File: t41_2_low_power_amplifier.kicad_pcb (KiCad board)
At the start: 2 copper layers, 100 x 76.2 mm, 61 parts, among them J1 5-1814832-1, J2 5-1814832-1, J3 B2B-XH-A_LF__SN_, J5 Screw_Terminal_01x02, Q1 Q_NPN_BCE, Q4 Q_NPN_BCE, Q5 Q_PMOS_GSD, Q6 Q_NPN_BEC, Q7 Q_NPN_BEC, Q8 Q_NPN_BEC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

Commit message: First version complete and sent to fab.
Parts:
- removed L2: ~, Binocular_Core:BN-43-202_VERTICAL
- added Q2: Q_NPN_BEC, Package_TO_SOT_SMD:SOT-23-3, F.Cu at (154.7, 96.6)
- added Q3: Q_PMOS_GSD, Package_TO_SOT_SMD:SOT-23-3, F.Cu at (160.1, 95.5)
- added R14: 10k, Resistor_SMD:R_1206_3216Metric, F.Cu at (132.5, 93.0)
- added R24: 10k, Resistor_SMD:R_1206_3216Metric, F.Cu at (149.2, 95.6)
- added R27: 10k, Resistor_SMD:R_1206_3216Metric, F.Cu at (159.5, 99.6)
- moved J1 16.0 mm to (187.1, 71.5)
- moved T1 12.3 mm to (172.6, 74.5)
- moved C1 2.61 mm to (168.3, 74.5), turned to 0 degrees
- moved C18 0.72 mm to (143.9, 60.4), turned to 180 degrees
- moved C15 0.25 mm to (125.9, 76.1)
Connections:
- C1 pad 1: /12V_IN_FIL -> /12V_FINAL
- T1 pad 4: /12V_IN_FIL -> /12V_FINAL
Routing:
- net /8V: track 9.43 -> 43.3 mm
- net /12V_FINAL: track 0.00 -> 27.0 mm
- net /12V: track 51.6 -> 75.9 mm
- net Net-(T1-AB): track 0.00 -> 6.57 mm
- net Net-(Q2-C): track 0.00 -> 6.32 mm
- net Net-(Q7-C): track 12.5 -> 18.6 mm
- net Net-(R11-Pad2): track 0.00 -> 4.71 mm
- net /TXRX: track 44.8 -> 48.5 mm
- net Net-(Q4-C): track 4.50 -> 7.95 mm
- net Net-(Q1-C): track 4.55 -> 7.97 mm
- net Net-(T3-AB): track 0.00 -> 3.28 mm
- net Net-(T3-SB): track 0.00 -> 3.00 mm
- net Net-(T3-SA): track 0.00 -> 2.94 mm
- net Net-(Q2-B): track 0.00 -> 2.92 mm
- net /12V_IN_FIL: track 6.26 -> 8.60 mm
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
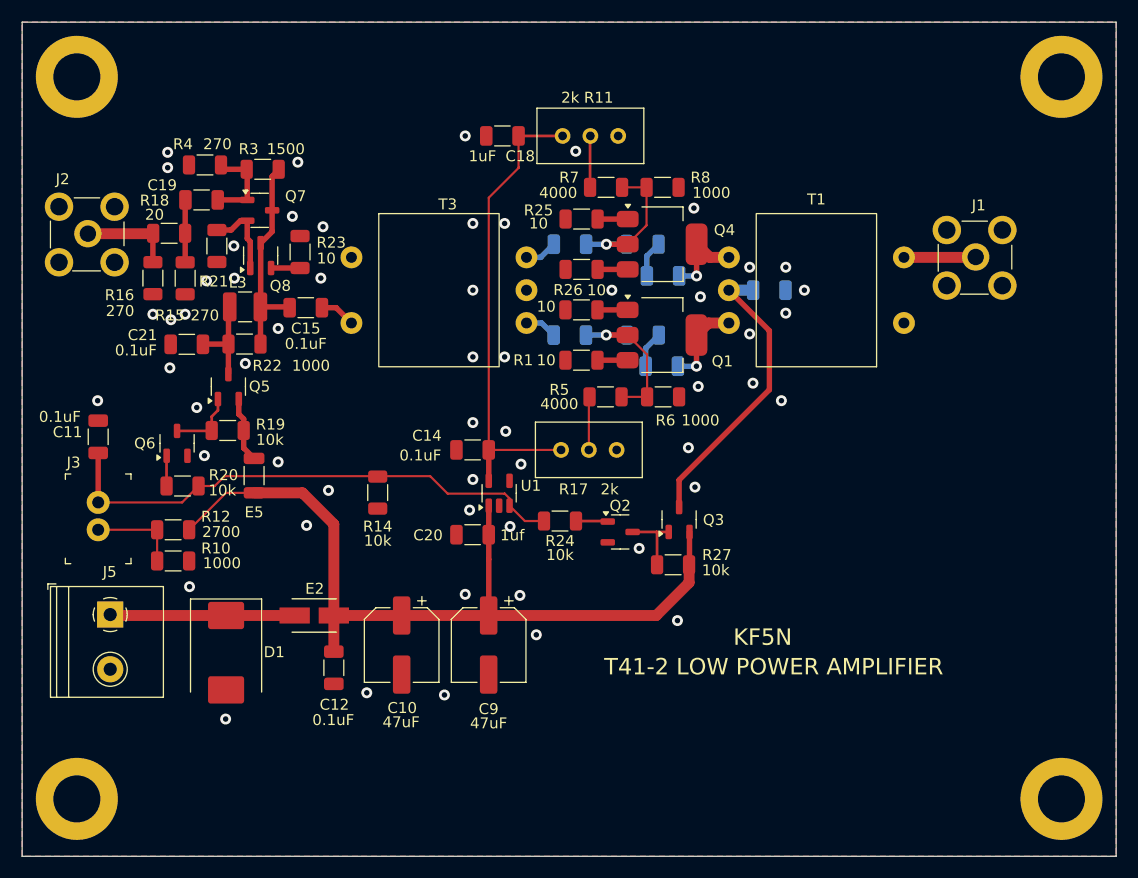
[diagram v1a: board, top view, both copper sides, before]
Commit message: Most routing completed.
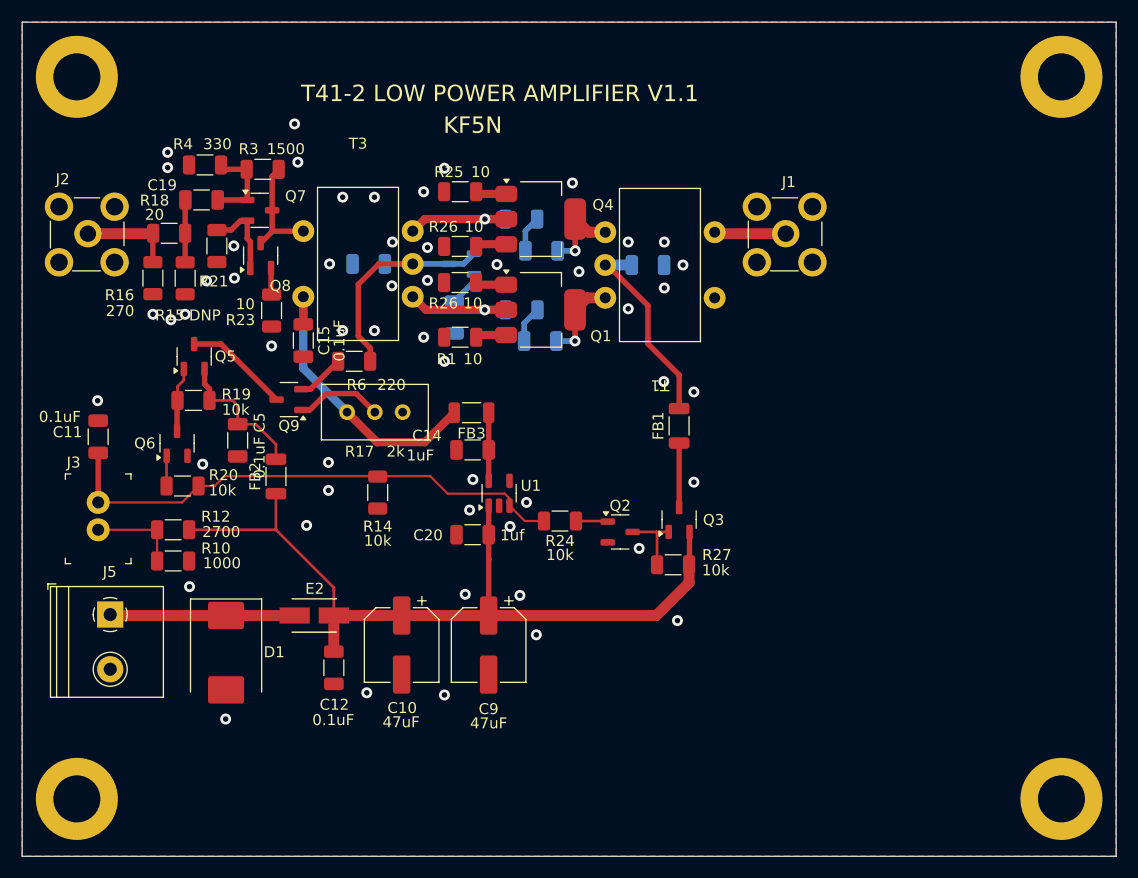
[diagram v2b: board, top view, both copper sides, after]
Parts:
- removed C18: 1uF, Capacitor_SMD:C_1206_3216Metric
- removed C21, C6: 0.1uF, Capacitor_SMD:C_1206_3216Metric
- removed E5: XXX, Inductor_SMD:L_1206_3216Metric
- removed L3: 10uH, Inductor_SMD:L_1210_3225Metric
- removed R11: 2k, Potentiometer_THT:Potentiometer_Bourns_3296W_Vertical
- removed R22, R8: 1000, Resistor_SMD:R_1206_3216Metric
- removed R7: 4000, Resistor_SMD:R_1206_3216Metric
- added C4: 0.1uF, Capacitor_SMD:C_1206_3216Metric, B.Cu at (131.7, 72.1)
- added FB1: FerriteBead_Small, Inductor_SMD:L_1206_3216Metric, F.Cu at (160.1, 86.9)
- added FB2: FerriteBead_Small, Inductor_SMD:L_1206_3216Metric, F.Cu at (123.2, 91.5)
- added FB3: FerriteBead_Small, Inductor_SMD:L_1206_3216Metric, F.Cu at (141.1, 85.7)
- added Q10: Q_NPN_BEC, Package_TO_SOT_SMD:SOT-23-3, B.Cu at (140.2, 72.1)
- added Q9: Q_NPN_BEC, Package_TO_SOT_SMD:SOT-23-3, F.Cu at (124.4, 84.5)
- C14: value 0.1uF -> 1uF
- C5: moved to F.Cu
- R15: value 270 -> DNP
- R2, R9: value 5 -> 680
- R4: value 270 -> 330
- R5: value 4000 -> 51; moved to B.Cu
- R6: value 1000 -> 220
- T1, T3: footprint Binocular_Core:BN-43-302 -> Binocular_Core:BN-43-302_Vertical
- moved C5 35.3 mm to (119.7, 88.2), turned to -90 degrees
- moved R6 28.4 mm to (130.3, 81.0)
- moved R17 19.9 mm to (129.7, 85.7)
- moved J1 17.5 mm to (169.7, 69.4)
- moved R5 15.6 mm to (139.5, 77.0), turned to 90 degrees
- moved T1 14.5 mm to (158.3, 72.2)
- moved R25 11.4 mm to (140.0, 65.5)
- moved R26 11.4 mm to (140.0, 73.8)
- moved C1 11.3 mm to (157.2, 72.2)
- moved Q1 11.3 mm to (147.4, 76.3)
- moved R2 11.3 mm to (145.6, 76.3)
- moved C2 11.3 mm to (147.5, 70.9)
- moved C3 11.3 mm to (147.4, 79.2)
- moved Q4 11.3 mm to (147.4, 68.0)
- moved R9 11.3 mm to (145.6, 68.0)
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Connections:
- C14 pad 1: /8V -> Net-(U1-VOUT)
- C15 pad 1: Net-(T3-AB) -> /10V_REG
- C15 pad 2: Net-(Q7-C) -> GND
- C5 pad 1: Net-(Q4-B) -> Net-(Q5-S)
- C5 pad 2: Net-(T3-SB) -> GND
- Q3 pad 3: /12V_FINAL -> Net-(Q3-D)
- R17 pad 1: /8V -> /10V_REG
- R17 pad 2: Net-(R17-Pad2) -> Net-(Q9-B)
- R5 pad 1: Net-(R17-Pad2) -> GND
- R5 pad 2: Net-(Q1-B) -> Net-(Q10-E)
- R6 pad 1: GND -> /BASE_BIAS
- R6 pad 2: Net-(Q1-B) -> Net-(Q9-E)
- T3 pad 1: GND -> Net-(Q7-C)
- T3 pad 2: Net-(T3-AB) -> /10V_REG
- T3 pad 3: Net-(T3-SA) -> Net-(Q1-B)
- T3 pad 4: GND -> /BASE_BIAS
- T3 pad 5: Net-(T3-SB) -> Net-(Q4-B)
- U1 pad 5: /8V -> Net-(U1-VOUT)
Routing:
- net /8V: track 43.3 -> 0.00 mm
- net /10V_REG: track 0.00 -> 26.8 mm
- net /BASE_BIAS: track 0.00 -> 21.8 mm
- net /12V_FINAL: track 27.0 -> 18.1 mm
- net Net-(Q7-C): track 18.6 -> 10.3 mm
- net Net-(Q9-B): track 0.00 -> 8.04 mm
- net Net-(Q5-S): track 6.00 -> 13.2 mm
- net Net-(U1-VOUT): track 0.00 -> 6.04 mm
- net Net-(Q3-D): track 0.00 -> 5.85 mm
- net Net-(R17-Pad2): track 4.88 -> 0.00 mm
- net Net-(R11-Pad2): track 4.71 -> 0.00 mm
- net Net-(Q9-E): track 0.00 -> 4.42 mm
- net Net-(Q1-B): track 14.4 -> 10.9 mm
- net Net-(T3-AB): track 3.28 -> 0.00 mm
- net Net-(Q10-E): track 0.00 -> 3.22 mm
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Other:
- board text added: "T41-2 LOW POWER AMPLIFIER V1.1"
- board text removed: "T41-2 LOW POWER AMPLIFIER"

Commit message: Low Power Amplifier ready for fab.
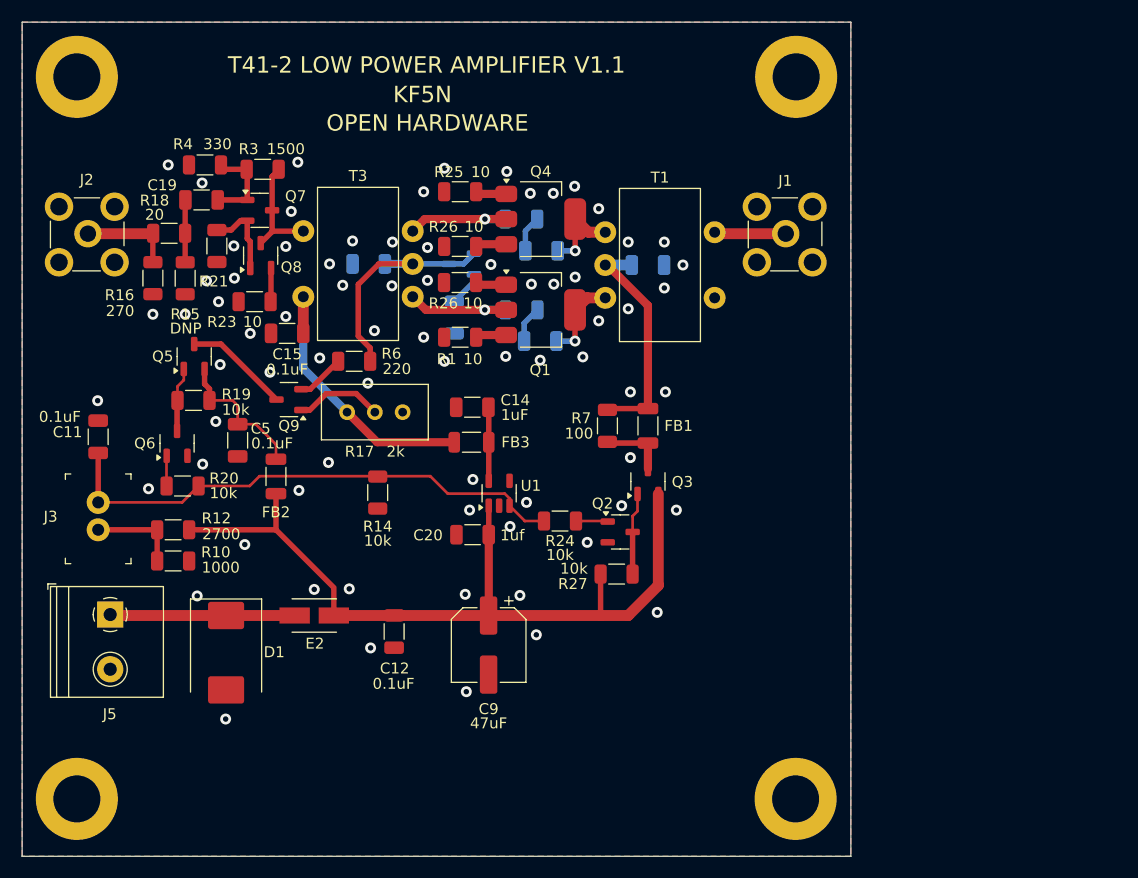
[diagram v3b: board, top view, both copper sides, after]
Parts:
- removed C10: 47uF, Capacitor_SMD:CP_Elec_6.3x5.7
- added R7: 100, Resistor_SMD:R_1206_3216Metric, F.Cu at (153.5, 86.9)
- moved H3 24.3 mm to (170.7, 121.0)
- moved H4 24.2 mm to (170.8, 55.0)
- moved C12 6.43 mm to (134.0, 105.7)
- moved R27 5.23 mm to (154.3, 100.5), turned to 180 degrees
- moved Q3 4.49 mm to (157.2, 92.0)
- moved C14 3.90 mm to (141.2, 85.2)
- moved FB1 2.85 mm to (157.2, 86.9)
- moved FB3 2.70 mm to (141.1, 88.4)
- moved R23 1.75 mm to (121.2, 75.5), turned to 0 degrees
- moved C15 1.61 mm to (124.2, 78.5), turned to 180 degrees
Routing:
- net /12V_FINAL: track 18.1 -> 20.6 mm
- net /12V: track 73.0 -> 74.3 mm
- net Net-(Q2-C): track 6.32 -> 7.51 mm
- net GND: vias 53 -> 74
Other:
- board size 100 x 76.2 mm -> 75.8 x 76.2 mm
- board text added: "OPEN HARDWARE"

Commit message: T41-2 Low Power Amplifier to fab.
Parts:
- removed Q2, Q6: Q_NPN_BEC, Package_TO_SOT_SMD:SOT-23-3
- removed Q3, Q5: Q_PMOS_GSD, Package_TO_SOT_SMD:SOT-23-3
- removed R10: 1000, Resistor_SMD:R_1206_3216Metric
- removed R12: 2700, Resistor_SMD:R_1206_3216Metric
- removed R19, R20, R24, R27: 10k, Resistor_SMD:R_1206_3216Metric
- removed U1: MCP1802x-xx02xOT, Package_TO_SOT_SMD:SOT-23-5
- added C6: 0.1uF, Capacitor_SMD:C_1206_3216Metric, F.Cu at (157.2, 92.3)
- added R8: 51, Resistor_SMD:R_1206_3216Metric, F.Cu at (139.5, 82.9)
- added U2: MCP1804x-C002xOT, Package_TO_SOT_SMD:SOT-23-5, F.Cu at (152.5, 91.5)
- added U3: MCP1804x-A002xOT, Package_TO_SOT_SMD:SOT-23-5, F.Cu at (123.0, 89.5)
- C11: value 0.1uF -> 0.01uF
- C14: value 1uF -> 0.1uF
- C20: value 1uf -> 0.1uF
- Q10, R5: moved to F.Cu
- R23: value 10 -> 4.7
- R3: value 1500 -> 1000
- R4: value 330 -> 180
- moved C5 28.9 mm to (148.3, 92.2)
- moved C20 24.7 mm to (117.9, 88.6)
- moved FB2 21.8 mm to (145.0, 92.2)
- moved C14 21.5 mm to (119.6, 85.0)
- moved R14 20.8 mm to (113.0, 85.9)
- moved FB3 17.9 mm to (123.9, 83.5), turned to 90 degrees
- moved Q10 12.2 mm to (145.1, 83.2), turned to 0 degrees
- moved H3 11.5 mm to (165.0, 111.0)
- moved R5 11.3 mm to (145.4, 86.7), turned to 180 degrees
- moved C9 10.5 mm to (138.1, 97.5)
- moved R6 10.4 mm to (139.5, 85.8)
- moved H2 10.0 mm to (105.0, 111.0)
- moved Q9 9.63 mm to (134.0, 85.0), turned to 90 degrees
- moved C12 9.60 mm to (132.3, 96.2)
- moved D1 9.45 mm to (118.6, 98.2)
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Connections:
- net Net-(Q3-D) renamed /12V_REG
- C14 pad 1: Net-(U1-VOUT) -> /10V_FIL
- FB3 pad 1: Net-(U1-VOUT) -> /10V_FIL
- J3 pad 2: Net-(J3-Pad2) -> GND
- Q10 pad 1: /BASE_BIAS -> Net-(Q10-B)
- Q10 pad 3: /BASE_BIAS -> Net-(Q10-B)
- Q9 pad 3: /12V_IN_FIL -> /10V_FIL
- R17 pad 1: /10V_REG -> /10V_FIL
- R6 pad 1: /BASE_BIAS -> Net-(Q10-B)
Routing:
- net /12V: track 74.3 -> 33.8 mm
- net /10V_REG: track 26.5 -> 7.55 mm
- net /10V_FIL: track 0.00 -> 17.2 mm
- net /TXRX: track 48.5 -> 64.4 mm, vias 0 -> 2
- net /12V_IN_FIL: track 9.68 -> 0.00 mm
- net Net-(Q10-B): track 0.00 -> 8.85 mm
- net Net-(J3-Pad2): track 8.24 -> 0.00 mm
- net Net-(Q2-C): track 7.51 -> 0.00 mm
- net Net-(U2-VIN): track 13.2 -> 6.27 mm
- net Net-(U1-VOUT): track 6.04 -> 0.00 mm
- net Net-(Q5-G): track 5.97 -> 0.00 mm
- net Net-(Q9-B): track 8.04 -> 4.36 mm
- net Net-(Q2-B): track 2.92 -> 0.00 mm
- net Net-(Q6-B): track 2.77 -> 0.00 mm
- net /12V_REG: track 6.12 -> 8.77 mm
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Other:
- board size 75.8 x 76.2 mm -> 70.1 x 66 mm
- board text added: "+"
- board text added: "-"
- board text added: "13.4 VOLTS"
- board text added: "BIAS ADJUST"
- board text added: "RF IN"
- board text added: "RF OUT"
- board text added: "T41-2 LOW POWER AMPLIFIER V1.2"
- board text added: "TXRX"
- board text removed: "T41-2 LOW POWER AMPLIFIER V1.1"

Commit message: Low Power Amplifier to fab.
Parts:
- removed E2: 28F0121-0SR-10, 28F0121_0SR_10:FB_28F0121-0SR-10
- added FB4: FerriteBead_Small, Inductor_SMD:L_1206_3216Metric, F.Cu at (126.9, 94.8)
- R14: value 10k -> 47k
- moved C6 3.92 mm to (160.2, 89.8)
- moved J1 2.84 mm to (164.5, 66.5)
- moved J5 0.95 mm to (109.0, 94.7)
- moved R7 0.06 mm to (157.2, 86.9)
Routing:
- net Net-(T1-AB): track 6.37 -> 8.19 mm
- net Net-(D1-K): track 17.0 -> 16.1 mm
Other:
- board text added: "10V"
- board text added: "12V"
- board text added: "IN"
- board text added: "T41-2 LOW POWER AMPLIFIER V1.3"
- board text removed: "T41-2 LOW POWER AMPLIFIER V1.2"

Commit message: Release to fab.
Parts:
- added R27: 10, Resistor_SMD:R_1206_3216Metric, F.Cu at (145.0, 97.6)
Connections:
- FB2 pad 1: /12V -> Net-(FB2-Pad1)
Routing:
- net Net-(FB2-Pad1): track 0.00 -> 2.35 mm
- net /12V: track 33.8 -> 35.9 mm
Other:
- board text added: "T41-2 LOW POWER AMPLIFIER V1.4"
- board text removed: "T41-2 LOW POWER AMPLIFIER V1.3"

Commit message: Updated schematic notes.
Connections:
- net /12V_FINAL renamed /10V_FINAL_REG
- net /12V_REG renamed Net-(U2-VOUT)
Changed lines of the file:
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@@
 	(net 11 "/12V")
 	(net 12 "Net-(Q7-C)")
-	(net 13 "/12V_REG")
+	(net 13 "/10V_FINAL_REG")
 	(net 14 "Net-(Q1-E)")
 	(net 15 "Net-(D1-K)")
 	(net 16 "Net-(Q9-E)")
-	(net 17 "/12V_FINAL")
+	(net 17 "Net-(U2-VOUT)")
 	(net 18 "Net-(J2-Pad2)")
 	(net 19 "Net-(Q9-B)")
@@
 			(layers "F.Cu" "F.Mask" "F.Paste")
 			(roundrect_rratio 0.238095)
-			(net 13 "/12V_REG")
+			(net 17 "Net-(U2-VOUT)")
 			(pintype "passive")
 		)
@@
 			(layers "F.Cu" "F.Mask" "F.Paste")
 			(roundrect_rratio 0.238095)
-			(net 17 "/12V_FINAL")
+			(net 13 "/10V_FINAL_REG")
 			(pintype "passive")
 		)
@@
 			(layers "F.Cu" "F.Mask" "F.Paste")
 			(roundrect_rratio 0.222222)
-			(net 17 "/12V_FINAL")
+			(net 13 "/10V_FINAL_REG")
 			(pintype "passive")
 		)
@@
 			(layers "F.Cu" "F.Mask" "F.Paste")
 			(roundrect_rratio 0.222222)
-			(net 13 "/12V_REG")
+			(net 17 "Net-(U2-VOUT)")
 			(pintype "passive")
 		)
@@
 			(layers "F.Cu" "F.Mask" "F.Paste")
 			(roundrect_rratio 0.217391)
-			(net 13 "/12V_REG")
+			(net 17 "Net-(U2-VOUT)")
 			(pintype "passive")
 		)
@@
 			(layers "F.Cu" "F.Mask" "F.Paste")
 			(roundrect_rratio 0.25)
-			(net 13 "/12V_REG")
+			(net 17 "Net-(U2-VOUT)")
 			(pinfunction "VOUT")
 			(pintype "power_out")
@@
 			(layers "*.Cu" "*.Mask")
 			(remove_unused_layers no)
-			(net 17 "/12V_FINAL")
+			(net 13 "/10V_FINAL_REG")
 			(pinfunction "SC")
 			(pintype "passive")
@@
 			(layers "B.Cu" "B.Mask" "B.Paste")
 			(roundrect_rratio 0.217391)
-			(net 17 "/12V_FINAL")
+			(net 13 "/10V_FINAL_REG")
 			(pintype "passive")
 		)
@@
 	)
 	(segment
-		(start 153.6 90.6)
-		(end 153.6 88.4625)
+		(start 157.2 85.325)
+		(end 153.6125 85.325)
 		(width 0.5)
 		(layer "F.Cu")
@@
 	)
 	(segment
-		(start 153.675 88.325)
-		(end 153.5 88.5)
-		(width 0.75)
-		(layer "F.Cu")
-		(net 13)
-	)
-	(segment
-		(start 157.2 88.325)
-		(end 153.675 88.325)
-		(width 0.75)
-		(layer "F.Cu")
-		(net 13)
-	)
-	(segment
-		(start 160.1875 88.2625)
-		(end 160.2 88.275)
+		(start 150.5 72.2)
+		(end 153.5 75.2)
 		(width 0.75)
 		(layer "F.Cu")
@@
 	)
 	(segment
-		(start 157.25 88.275)
-		(end 157.2 88.325)
+		(start 153.6125 85.325)
+		(end 153.5 85.4375)
 		(width 0.75)
 		(layer "F.Cu")
@@
 	)
 	(segment
-		(start 153.6125 88.475)
-		(end 153.5 88.3625)
-		(width 0.5)
-		(layer "F.Cu")
-		(net 13)
-	)
-	(segment
-		(start 160.2 88.275)
-		(end 157.25 88.275)
+		(start 153.5 85.4375)
+		(end 153.5 75.2)
 		(width 0.75)
 		(layer "F.Cu")
@@
 	)
 	(segment
-		(start 153.6 88.4625)
-		(end 153.5 88.3625)
-		(width 0.5)
-		(layer "F.Cu")
+		(start 152.725 72.2)
+		(end 150.5 72.2)
+		(width 1)
+		(layer "B.Cu")
 		(net 13)
 	)
@@
 	)
 	(segment
-		(start 157.2 85.325)
-		(end 153.6125 85.325)
+		(start 153.6 90.6)
+		(end 153.6 88.4625)
 		(width 0.5)
 		(layer "F.Cu")
@@
 	)
 	(segment
-		(start 150.5 72.2)
-		(end 153.5 75.2)
+		(start 153.675 88.325)
+		(end 153.5 88.5)
 		(width 0.75)
 		(layer "F.Cu")
@@
 	)
 	(segment
-		(start 153.6125 85.325)
-		(end 153.5 85.4375)
+		(start 157.2 88.325)
+		(end 153.675 88.325)
 		(width 0.75)
 		(layer "F.Cu")
@@
 	)
 	(segment
-		(start 153.5 85.4375)
-		(end 153.5 75.2)
+		(start 160.1875 88.2625)
+		(end 160.2 88.275)
 		(width 0.75)
 		(layer "F.Cu")
@@
 	)
 	(segment
-		(start 152.725 72.2)
-		(end 150.5 72.2)
-		(width 1)
-		(layer "B.Cu")
+		(start 157.25 88.275)
+		(end 157.2 88.325)
+		(width 0.75)
+		(layer "F.Cu")
+		(net 17)
+	)
+	(segment
+		(start 153.6125 88.475)
+		(end 153.5 88.3625)
+		(width 0.5)
+		(layer "F.Cu")
+		(net 17)
+	)
+	(segment
+		(start 160.2 88.275)
+		(end 157.25 88.275)
+		(width 0.75)
+		(layer "F.Cu")
+		(net 17)
+	)
+	(segment
+		(start 153.6 88.4625)
+		(end 153.5 88.3625)
+		(width 0.5)
+		(layer "F.Cu")
 		(net 17)
 	)

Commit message: Finishing up version 1.5.  Not ready for fab.
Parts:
- removed C9: 47uF, Capacitor_SMD:CP_Elec_6.3x5.7
- removed R27: 10, Resistor_SMD:R_1206_3216Metric
- removed U2: MCP1804x-C002xOT, Package_TO_SOT_SMD:SOT-23-5
- added C7: 0.1uF, Capacitor_SMD:C_1206_3216Metric, B.Cu at (154.6, 68.4)
- added C8: 0.1uF, Capacitor_SMD:C_1206_3216Metric, B.Cu at (154.5, 75.9)
- added L1: ~, Binocular_Core:FT37-43, F.Cu at (150.5, 72.2)
- added U1: MCP1804T-A002I/MT, footprints:SOT-89_5MC_MCH, F.Cu at (148.0, 93.1)
- C1: value 0.1uF -> 0.01uF
- C12, C20, C5: value 0.1uF -> 10uF
- moved C6 13.3 mm to (150.0, 98.2)
- moved J1 12.1 mm to (155.0, 59.0)
- moved FB2 9.50 mm to (135.9, 94.8), turned to 0 degrees
- moved T1 8.00 mm to (162.0, 72.2)
- moved C5 6.50 mm to (145.9, 98.2)
- moved C12 0.90 mm to (131.4, 96.3)
- moved R26 0.31 mm to (137.3, 73.8)
- moved R1 0.30 mm to (137.3, 78.8)
- moved R13 0.30 mm to (137.3, 70.5)
- moved R25 0.30 mm to (137.3, 65.5)
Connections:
- FB2 pad 1: Net-(FB2-Pad1) -> /12V
- T1 pad 3: Net-(Q4-C) -> Net-(T1-SA)
- T1 pad 4: /10V_FINAL_REG -> GND
- T1 pad 5: Net-(Q1-C) -> Net-(T1-SB)
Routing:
- net /12V: track 35.9 -> 22.7 mm
- net Net-(T1-AB): track 8.19 -> 17.2 mm
- net Net-(U1-VOUT): track 9.25 -> 15.9 mm
- net GND: track 0.00 -> 5.00 mm, vias 72 -> 90
- net Net-(U1-VIN): track 6.27 -> 11.2 mm
- net /TXRX: track 64.4 -> 60.5 mm
- net Net-(Q4-C): track 7.95 -> 10.9 mm
- net Net-(Q1-C): track 7.97 -> 10.8 mm
- net Net-(T1-SB): track 0.00 -> 2.79 mm
- net Net-(T1-SA): track 0.00 -> 2.76 mm
- net Net-(FB2-Pad1): track 2.35 -> 0.00 mm
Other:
- board text added: "T41-2 LOW POWER AMPLIFIER V1.5"
- board text removed: "12V"
- board text removed: "T41-2 LOW POWER AMPLIFIER V1.4"
